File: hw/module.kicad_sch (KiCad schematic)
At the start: 1 part

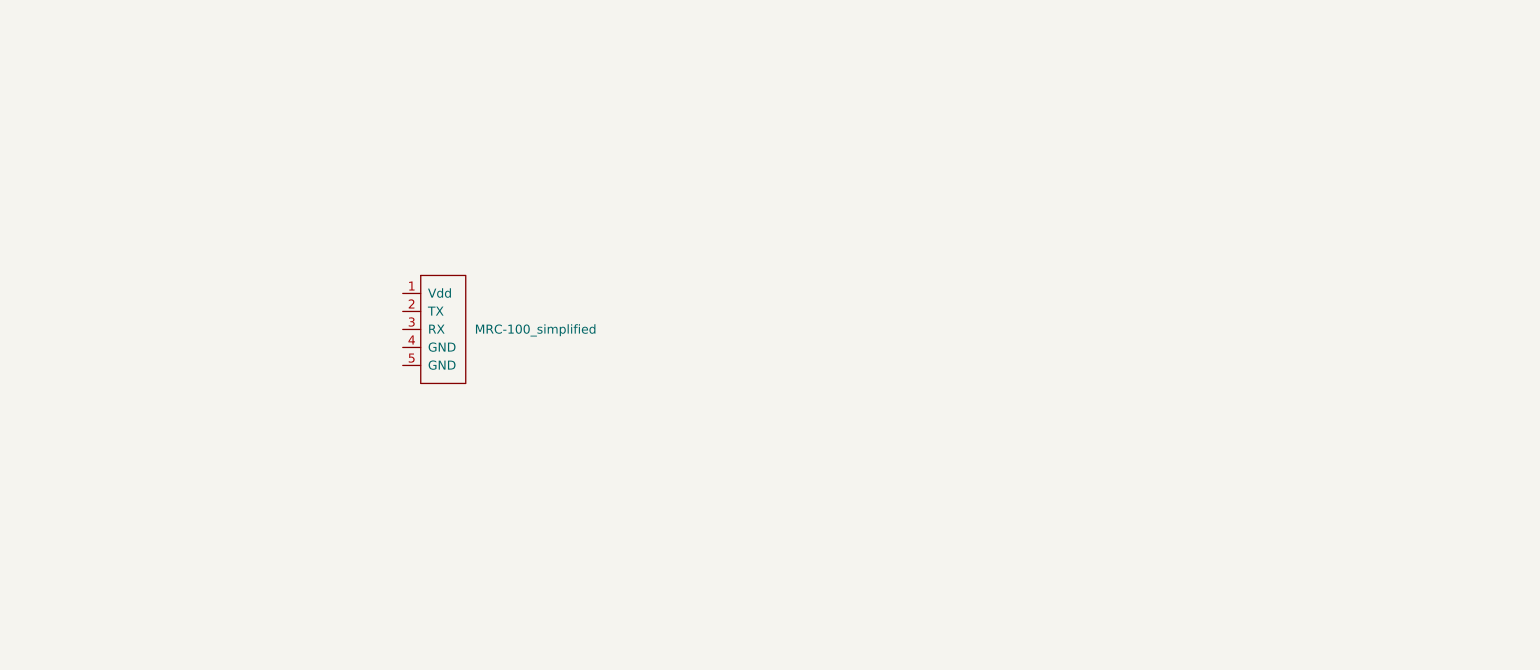
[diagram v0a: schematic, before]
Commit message: added stm_footprint
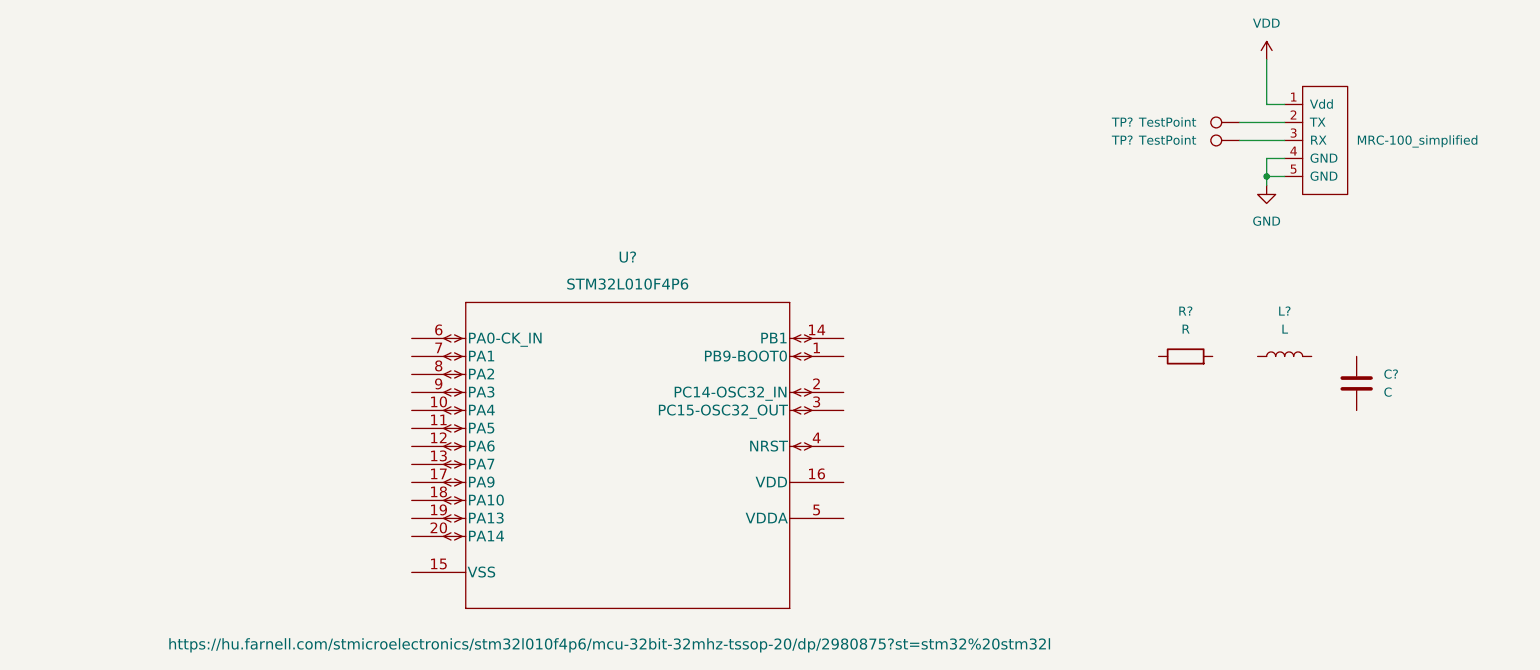
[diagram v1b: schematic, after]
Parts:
- added C?: C, symbol Device:C
- added L?: L, symbol Device:L
- added R?: R, symbol Device:R
- added TP? (x2): TestPoint, TestPoint:TestPoint_Pad_3.0x3.0mm, symbol Connector:TestPoint
- added U?: STM32L010F4P6, farnell:STM32L010F4P6, symbol farnell:STM32L010F4P6
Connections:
- net VDD: now reaches Int1.1 (Vdd)
- net at Int1.2 (TX): now also TP?.1
- net at Int1.3 (RX): now also TP?.1
- net GND: now reaches Int1.4 (GND)
- net GND: now also Int1.5 (GND)
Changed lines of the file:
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@@
 (kicad_sch (version 20211123) (generator eeschema)
   (paper "A4")
-  (symbol (lib_id "BME:MRC-100_simplified") (at 90.17 91.44 0) (unit 1)
-    (in_bom yes) (on_board yes)
-    (property "Reference" "Int1" (id 0) (at 90.17 80.01 0)
-      (effects (font (size 1.27 1.27)) hide)
-    )
-    (property "Value" "MRC-100_simplified" (id 1) (at 96.52 91.4399 0)
+  (junction (at 208.28 69.85) (diameter 0) (color 0 0 0 0)
+  )
+  (wire (pts (xy 204.47 62.23) (xy 210.82 62.23))
+    (stroke (width 0) (type default) (color 0 0 0 0))
+  )
+  (wire (pts (xy 208.28 53.34) (xy 208.28 59.69))
+    (stroke (width 0) (type default) (color 0 0 0 0))
+  )
+  (wire (pts (xy 208.28 67.31) (xy 208.28 69.85))
+    (stroke (width 0) (type default) (color 0 0 0 0))
+  )
+  (wire (pts (xy 208.28 69.85) (xy 208.28 71.12))
+    (stroke (width 0) (type default) (color 0 0 0 0))
+  )
+  (wire (pts (xy 204.47 64.77) (xy 210.82 64.77))
+    (stroke (width 0) (type default) (color 0 0 0 0))
+  )
+  (wire (pts (xy 210.82 69.85) (xy 208.28 69.85))
+    (stroke (width 0) (type default) (color 0 0 0 0))
+  )
+  (wire (pts (xy 208.28 59.69) (xy 210.82 59.69))
+    (stroke (width 0) (type default) (color 0 0 0 0))
+  )
+  (wire (pts (xy 210.82 67.31) (xy 208.28 67.31))
+    (stroke (width 0) (type default) (color 0 0 0 0))
+  )
+  (symbol (lib_id "power:VDD") (at 208.28 53.34 0) (unit 1)
+    (in_bom yes) (on_board yes) (fields_autoplaced)
+    (property "Reference" "#PWR?" (id 0) (at 208.28 57.15 0)
+      (effects (font (size 1.27 1.27)) hide)
+    )
+    (property "Value" "VDD" (id 1) (at 208.28 48.26 0))
+    (property "Footprint" "" (id 2) (at 208.28 53.34 0)
+      (effects (font (size 1.27 1.27)) hide)
+    )
+    (property "Datasheet" "" (id 3) (at 208.28 53.34 0)
+      (effects (font (size 1.27 1.27)) hide)
+    )
+    (pin "1")
+  )
+  (symbol (lib_id "power:GND") (at 208.28 71.12 0) (unit 1)
+    (in_bom yes) (on_board yes) (fields_autoplaced)
+    (property "Reference" "#PWR?" (id 0) (at 208.28 77.47 0)
+      (effects (font (size 1.27 1.27)) hide)
+    )
+    (property "Value" "GND" (id 1) (at 208.28 76.2 0))
+    (property "Footprint" "" (id 2) (at 208.28 71.12 0)
+      (effects (font (size 1.27 1.27)) hide)
+    )
+    (property "Datasheet" "" (id 3) (at 208.28 71.12 0)
+      (effects (font (size 1.27 1.27)) hide)
+    )
+    (pin "1")
+  )
+  (symbol (lib_id "Device:L") (at 210.82 95.25 90) (unit 1)
+    (in_bom yes) (on_board yes) (fields_autoplaced)
+    (property "Reference" "L?" (id 0) (at 210.82 88.9 90))
+    (property "Value" "L" (id 1) (at 210.82 91.44 90))
+    (property "Footprint" "" (id 2) (at 210.82 95.25 0)
+      (effects (font (size 1.27 1.27)) hide)
+    )
+    (property "Datasheet" "~" (id 3) (at 210.82 95.25 0)
+      (effects (font (size 1.27 1.27)) hide)
+    )
+    (pin "1")
+    (pin "2")
+  )
+  (symbol (lib_id "Device:R") (at 196.85 95.25 90) (unit 1)
+    (in_bom yes) (on_board yes) (fields_autoplaced)
+    (property "Reference" "R?" (id 0) (at 196.85 88.9 90))
+    (property "Value" "R" (id 1) (at 196.85 91.44 90))
+    (property "Footprint" "" (id 2) (at 196.85 97.028 90)
+      (effects (font (size 1.27 1.27)) hide)
+    )
+    (property "Datasheet" "~" (id 3) (at 196.85 95.25 0)
+      (effects (font (size 1.27 1.27)) hide)
+    )
+    (pin "1")
+    (pin "2")
+  )
+  (symbol (lib_id "BME:MRC-100_simplified") (at 214.63 64.77 0) (unit 1)
+    (in_bom yes) (on_board yes)
+    (property "Reference" "Int1" (id 0) (at 214.63 53.34 0)
+      (effects (font (size 1.27 1.27)) hide)
+    )
+    (property "Value" "MRC-100_simplified" (id 1) (at 220.98 64.7699 0)
       (effects (font (size 1.27 1.27)) (justify left))
     )
-    (property "Footprint" "BME:mrc-100" (id 2) (at 92.71 83.82 0)
+    (property "Footprint" "BME:mrc-100" (id 2) (at 217.17 57.15 0)
       (effects (font (size 2.9972 2.9972)) hide)
     )
-    (property "Datasheet" "" (id 3) (at 92.71 83.82 0)
+    (property "Datasheet" "" (id 3) (at 217.17 57.15 0)
       (effects (font (size 2.9972 2.9972)) hide)
     )
@@
     (pin "5")
   )
+  (symbol (lib_id "Connector:TestPoint") (at 204.47 64.77 90) (unit 1)
+    (in_bom yes) (on_board yes)
+    (property "Reference" "TP?" (id 0) (at 187.96 64.77 90))
+    (property "Value" "TestPoint" (id 1) (at 194.31 64.77 90))
+    (property "Footprint" "TestPoint:TestPoint_Pad_3.0x3.0mm" (id 2) (at 204.47 59.69 0)
+      (effects (font (size 1.27 1.27)) hide)
+    )
+    (property "Datasheet" "~" (id 3) (at 204.47 59.69 0)
+      (effects (font (size 1.27 1.27)) hide)
+    )
+    (pin "1")
+  )
+  (symbol (lib_id "Connector:TestPoint") (at 204.47 62.23 90) (unit 1)
+    (in_bom yes) (on_board yes)
+    (property "Reference" "TP?" (id 0) (at 187.96 62.23 90))
+    (property "Value" "TestPoint" (id 1) (at 194.31 62.23 90))
+    (property "Footprint" "TestPoint:TestPoint_Pad_3.0x3.0mm" (id 2) (at 204.47 57.15 0)
+      (effects (font (size 1.27 1.27)) hide)
+    )
+    (property "Datasheet" "~" (id 3) (at 204.47 57.15 0)
+      (effects (font (size 1.27 1.27)) hide)
+    )
+    (pin "1")
+  )
+  (symbol (lib_id "farnell:STM32L010F4P6") (at 87.63 92.71 0) (unit 1)
+    (in_bom yes) (on_board yes)
+    (property "Reference" "U?" (id 0) (at 118.11 81.28 0)
+      (effects (font (size 1.524 1.524)))
+    )
+    (property "Value" "STM32L010F4P6" (id 1) (at 118.11 85.09 0)
+      (effects (font (size 1.524 1.524)))
+    )
+    (property "Footprint" "farnell:STM32L010F4P6" (id 2) (at 118.11 86.614 0)
+      (effects (font (size 1.524 1.524)) hide)
+    )
+    (property "Datasheet" "https://hu.farnell.com/stmicroelectronics/stm32l010f4p6/mcu-32bit-32mhz-tssop-20/dp/2980875?st=stm32%20stm32l" (id 3) (at 115.57 135.89 0)
+      (effects (font (size 1.524 1.524)))
+    )
+    (pin "1")
+    (pin "10")
+    (pin "11")
+    (pin "12")
+    (pin "13")
+    (pin "14")
+    (pin "15")
+    (pin "16")
+    (pin "17")
+    (pin "18")
+    (pin "19")
+    (pin "2")
+    (pin "20")
+    (pin "3")
+    (pin "4")
+    (pin "5")
+    (pin "6")
+    (pin "7")
+    (pin "8")
+    (pin "9")
+  )
+  (symbol (lib_id "Device:C") (at 220.98 99.06 0) (unit 1)
+    (in_bom yes) (on_board yes) (fields_autoplaced)
+    (property "Reference" "C?" (id 0) (at 224.79 97.7899 0)
+      (effects (font (size 1.27 1.27)) (justify left))
+    )
+    (property "Value" "C" (id 1) (at 224.79 100.3299 0)
+      (effects (font (size 1.27 1.27)) (justify left))
+    )
+    (property "Footprint" "" (id 2) (at 221.9452 102.87 0)
+      (effects (font (size 1.27 1.27)) hide)
+    )
+    (property "Datasheet" "~" (id 3) (at 220.98 99.06 0)
+      (effects (font (size 1.27 1.27)) hide)
+    )
+    (pin "1")
+    (pin "2")
+  )
   (sheet_instances
     (path "/" (page "1"))
   )
   (symbol_instances
+    (path "/17bb3b8c-d172-4586-b519-aaef979fe74e"
+      (reference "#PWR?") (unit 1) (value "VDD") (footprint "")
+    )
+    (path "/1cfa9e16-b159-4ea2-840d-4104183feb20"
+      (reference "#PWR?") (unit 1) (value "GND") (footprint "")
+    )
+    (path "/e710ed9f-ec1f-4783-b4a0-d98dfbd2e493"
+      (reference "C?") (unit 1) (value "C") (footprint "")
+    )
     (path "/5460b77d-1803-489d-8702-1c9b3487aa2e"
       (reference "Int1") (unit 1) (value "MRC-100_simplified") (footprint "BME:mrc-100")
     )
-  )
+    (path "/1d9087ab-8143-4f4f-9f03-1568f6982bbf"
+      (reference "L?") (unit 1) (value "L") (footprint "")
+    )
+    (path "/3b5914d8-e3c0-4a01-a39d-adaadd543be4"
+      (reference "R?") (unit 1) (value "R") (footprint "")
+    )
+    (path "/5d21b345-4fa1-4932-8588-fe8d06de0db6"
+      (reference "TP?") (unit 1) (value "TestPoint") (footprint "TestPoint:TestPoint_Pad_3.0x3.0mm")
+    )
+    (path "/6246fa84-5bf9-4415-acdd-f2ce3a6d0609"
+      (reference "TP?") (unit 1) (value "TestPoint") (footprint "TestPoint:TestPoint_Pad_3.0x3.0mm")
+    )
+    (path "/c3a09ed2-f9ee-4187-a81e-7663ad390909"
+      (reference "U?") (unit 1) (value "STM32L010F4P6") (footprint "farnell:STM32L010F4P6")
+    )
+  )
